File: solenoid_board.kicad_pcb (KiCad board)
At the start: 2 copper layers, 100 x 93 mm, 38 parts, among them J2 MCU_LEFT_LEGS, J3 MCU_RIGHT_LEGS

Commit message: Added Mounting holes
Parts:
- added REF**: MountingHole_2.7mm_M2.5, MountingHole:MountingHole_2.7mm_M2.5, F.Cu at (187.0, 142.0)
- added REF**: MountingHole_2.7mm_M2.5, MountingHole:MountingHole_2.7mm_M2.5, F.Cu at (97.0, 142.0)
- added REF**: MountingHole_2.7mm_M2.5, MountingHole:MountingHole_2.7mm_M2.5, F.Cu at (97.0, 57.0)
- added REF**: MountingHole_2.7mm_M2.5, MountingHole:MountingHole_2.7mm_M2.5, F.Cu at (187.0, 57.0)
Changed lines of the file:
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@@
     (tracks 307)
     (zones 0)
-    (modules 38)
+    (modules 42)
     (nets 46)
   )
@@
     (uvia_drill 0.1)
     (add_net +48V)
+  )
+  (module MountingHole:MountingHole_2.7mm_M2.5 (layer F.Cu)
+    (at 187 142)
+    (descr "Mounting Hole 2.7mm, no annular, M2.5")
+    (tags "mounting hole 2.7mm no annular m2.5")
+    (attr virtual)
+    (fp_text reference REF** (at 0 -3.7) (layer F.SilkS) hide
+      (effects (font (size 1 1) (thickness 0.15)))
+    )
+    (fp_text value MountingHole_2.7mm_M2.5 (at 0 3.7) (layer F.Fab) hide
+      (effects (font (size 1 1) (thickness 0.15)))
+    )
+    (fp_circle (center 0 0) (end 2.95 0) (layer F.CrtYd) (width 0.05))
+    (fp_circle (center 0 0) (end 2.7 0) (layer Cmts.User) (width 0.15))
+    (fp_text user %R (at 0.3 0) (layer F.Fab) hide
+      (effects (font (size 1 1) (thickness 0.15)))
+    )
+    (pad 1 np_thru_hole circle (at 0 0) (size 2.7 2.7) (drill 2.7) (layers *.Cu *.Mask))
+  )
+  (module MountingHole:MountingHole_2.7mm_M2.5 (layer F.Cu)
+    (at 97 142)
+    (descr "Mounting Hole 2.7mm, no annular, M2.5")
+    (tags "mounting hole 2.7mm no annular m2.5")
+    (attr virtual)
+    (fp_text reference REF** (at 0 -3.7) (layer F.SilkS) hide
+      (effects (font (size 1 1) (thickness 0.15)))
+    )
+    (fp_text value MountingHole_2.7mm_M2.5 (at 0 3.7) (layer F.Fab) hide
+      (effects (font (size 1 1) (thickness 0.15)))
+    )
+    (fp_circle (center 0 0) (end 2.95 0) (layer F.CrtYd) (width 0.05))
+    (fp_circle (center 0 0) (end 2.7 0) (layer Cmts.User) (width 0.15))
+    (fp_text user %R (at 0.3 0) (layer F.Fab) hide
+      (effects (font (size 1 1) (thickness 0.15)))
+    )
+    (pad 1 np_thru_hole circle (at 0 0) (size 2.7 2.7) (drill 2.7) (layers *.Cu *.Mask))
+  )
+  (module MountingHole:MountingHole_2.7mm_M2.5 (layer F.Cu)
+    (at 97 57)
+    (descr "Mounting Hole 2.7mm, no annular, M2.5")
+    (tags "mounting hole 2.7mm no annular m2.5")
+    (attr virtual)
+    (fp_text reference REF** (at 0 -3.7) (layer F.SilkS) hide
+      (effects (font (size 1 1) (thickness 0.15)))
+    )
+    (fp_text value MountingHole_2.7mm_M2.5 (at 0 3.7) (layer F.Fab) hide
+      (effects (font (size 1 1) (thickness 0.15)))
+    )
+    (fp_circle (center 0 0) (end 2.95 0) (layer F.CrtYd) (width 0.05))
+    (fp_circle (center 0 0) (end 2.7 0) (layer Cmts.User) (width 0.15))
+    (fp_text user %R (at 0.3 0) (layer F.Fab) hide
+      (effects (font (size 1 1) (thickness 0.15)))
+    )
+    (pad 1 np_thru_hole circle (at 0 0) (size 2.7 2.7) (drill 2.7) (layers *.Cu *.Mask))
+  )
+  (module MountingHole:MountingHole_2.7mm_M2.5 (layer F.Cu)
+    (at 187 57)
+    (descr "Mounting Hole 2.7mm, no annular, M2.5")
+    (tags "mounting hole 2.7mm no annular m2.5")
+    (attr virtual)
+    (fp_text reference REF** (at 0 -3.7) (layer F.SilkS) hide
+      (effects (font (size 1 1) (thickness 0.15)))
+    )
+    (fp_text value MountingHole_2.7mm_M2.5 (at 0 3.7) (layer F.Fab) hide
+      (effects (font (size 1 1) (thickness 0.15)))
+    )
+    (fp_circle (center 0 0) (end 2.95 0) (layer F.CrtYd) (width 0.05))
+    (fp_circle (center 0 0) (end 2.7 0) (layer Cmts.User) (width 0.15))
+    (fp_text user %R (at 0.3 0) (layer F.Fab) hide
+      (effects (font (size 1 1) (thickness 0.15)))
+    )
+    (pad 1 np_thru_hole circle (at 0 0) (size 2.7 2.7) (drill 2.7) (layers *.Cu *.Mask))
   )
   (module Resistor_THT:R_Axial_DIN0309_L9.0mm_D3.2mm_P20.32mm_Horizontal (layer F.Cu)
@@
   (segment (start 115.508999 115.127999) (end 115.4684 115.0874) (width 0.25) (layer F.Cu) (net 45))
   (segment (start 125.7681 115.127999) (end 115.508999 115.127999) (width 0.25) (layer F.Cu) (net 45))
-  (zone (net 13) (net_name GND) (layer B.Cu) (hatch edge 0.508)
-    (connect_pads (clearance 0.508))
-    (min_thickness 0.254)
-    (fill yes (arc_segments 32) (thermal_gap 0.508) (thermal_bridge_width 0.508))
-    (polygon
-      (pts
-        (xy 170.9928 55.0672) (xy 170.561 68.199) (xy 183.6928 68.834) (xy 183.6928 72.0598) (xy 171.6278 73.787)
-        (xy 170.9928 143.9672) (xy 93.726 143.7386) (xy 93.929142 55.092542) (xy 93.9038 55.0672) (xy 93.9546 55.0672)
-        (xy 93.9546 55.0418)
-      )
-    )
-  )
   (zone (net 26) (net_name +48V) (layer B.Cu) (hatch edge 0.508)
     (connect_pads (clearance 0.508))
@@
       )
     )
+  )
+  (zone (net 13) (net_name GND) (layer B.Cu) (hatch edge 0.508)
+    (connect_pads (clearance 0.508))
+    (min_thickness 0.254)
+    (fill yes (arc_segments 32) (thermal_gap 0.508) (thermal_bridge_width 0.508))
+    (polygon
+      (pts
+        (xy 169.5958 68.1482) (xy 183.3626 68.3768) (xy 183.6166 68.5292) (xy 183.515 68.5292) (xy 183.4896 68.58)
+        (xy 183.515279 68.618519) (xy 183.5404 72.0852) (xy 170.7642 72.1614) (xy 170.3578 134.62) (xy 103.9876 136.6012)
+        (xy 101.8032 56.0832) (xy 168.9354 55.6514)
+      )
+    )
+    (polygon
+      (pts
+        (xy 183.5404 68.6562) (xy 183.515279 68.618519) (xy 183.515 68.58)
+      )
+    )

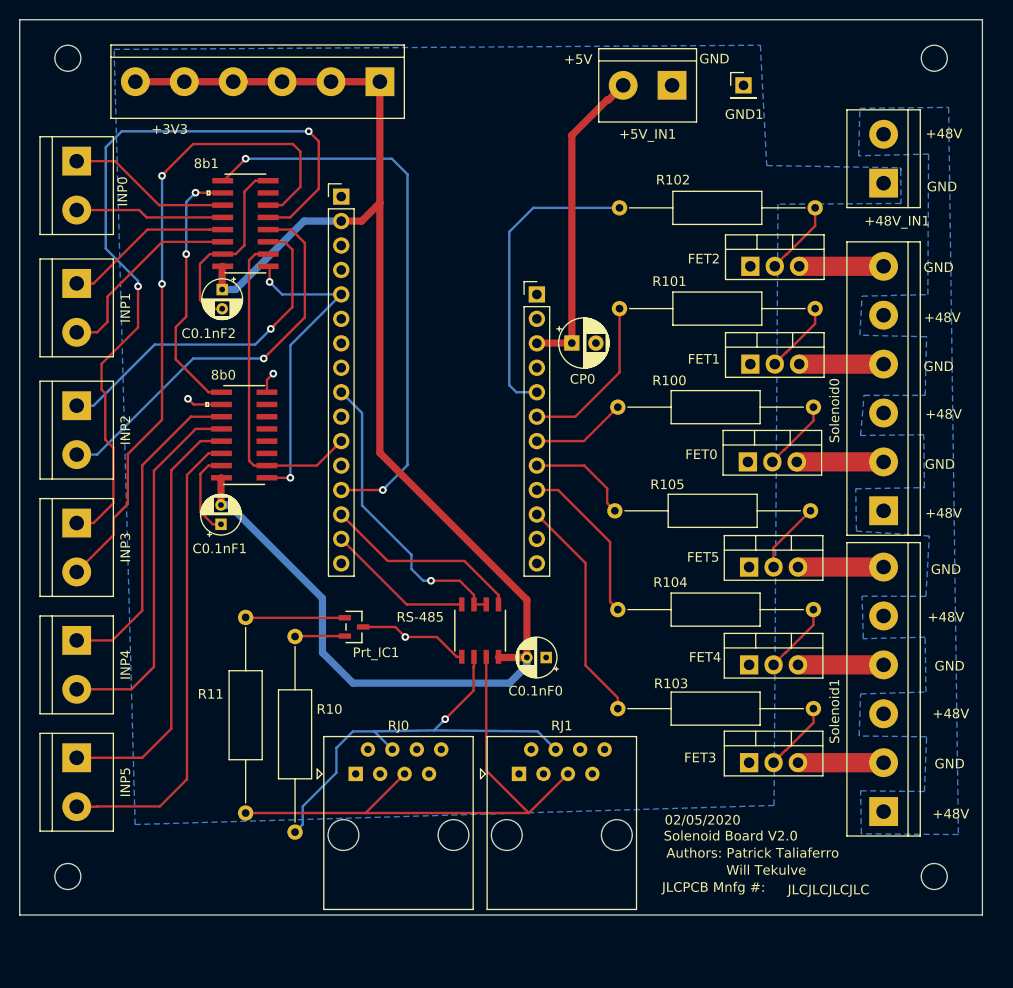
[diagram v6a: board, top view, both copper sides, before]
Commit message: Need to: (0) Use thicker traces, (1) Substitute +48V backplane with a wire in the bottom layer, (2) Substitute the screw terminals with pin headers.
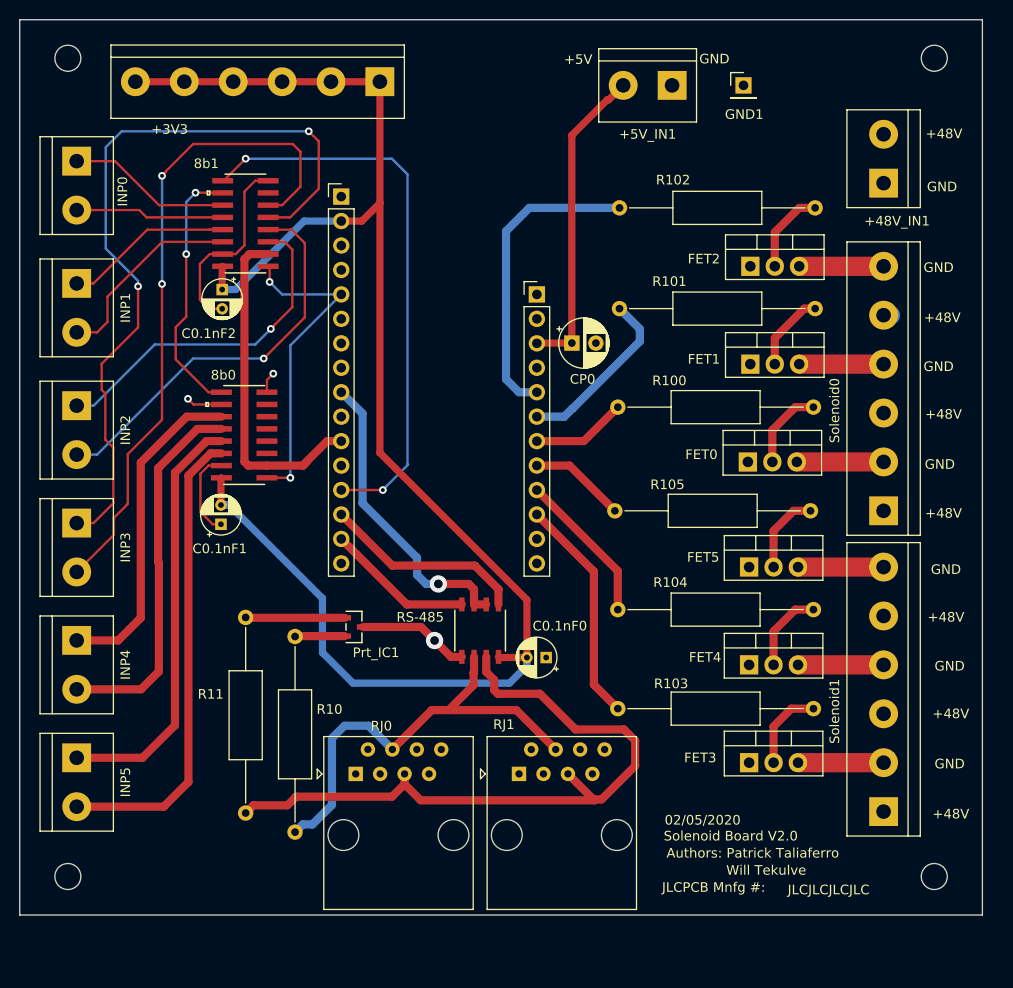
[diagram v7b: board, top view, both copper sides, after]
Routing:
- net /RJ45_5: track 59.0 -> 72.1 mm
- net Net-(FET3-Pad2): track 7.36 -> 8.67 mm
- net /D6: track 17.2 -> 15.9 mm
- net /SCK: track 33.9 -> 35.0 mm
- net /D11: track 17.1 -> 18.2 mm
- net Net-(FET4-Pad2): track 7.48 -> 8.56 mm
- net Net-(FET0-Pad2): track 7.48 -> 8.56 mm
- net +48V: track 0.00 -> 1.07 mm
- net Net-(FET5-Pad2): track 7.43 -> 8.46 mm
- net Net-(FET2-Pad2): track 7.83 -> 8.77 mm
- net /D9: track 10.9 -> 10.0 mm
- net Net-(FET1-Pad2): track 7.53 -> 8.16 mm
- net /INP4_0: track 33.5 -> 34.1 mm
- net /INP4_1: track 38.2 -> 38.7 mm
- net /RJ45_4: vias 1 -> 0
- removed copper zone on B.Cu, net +48V
- removed copper zone on B.Cu, net GND
